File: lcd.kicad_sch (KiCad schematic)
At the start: 9 parts, among them J5 Conn_01x10

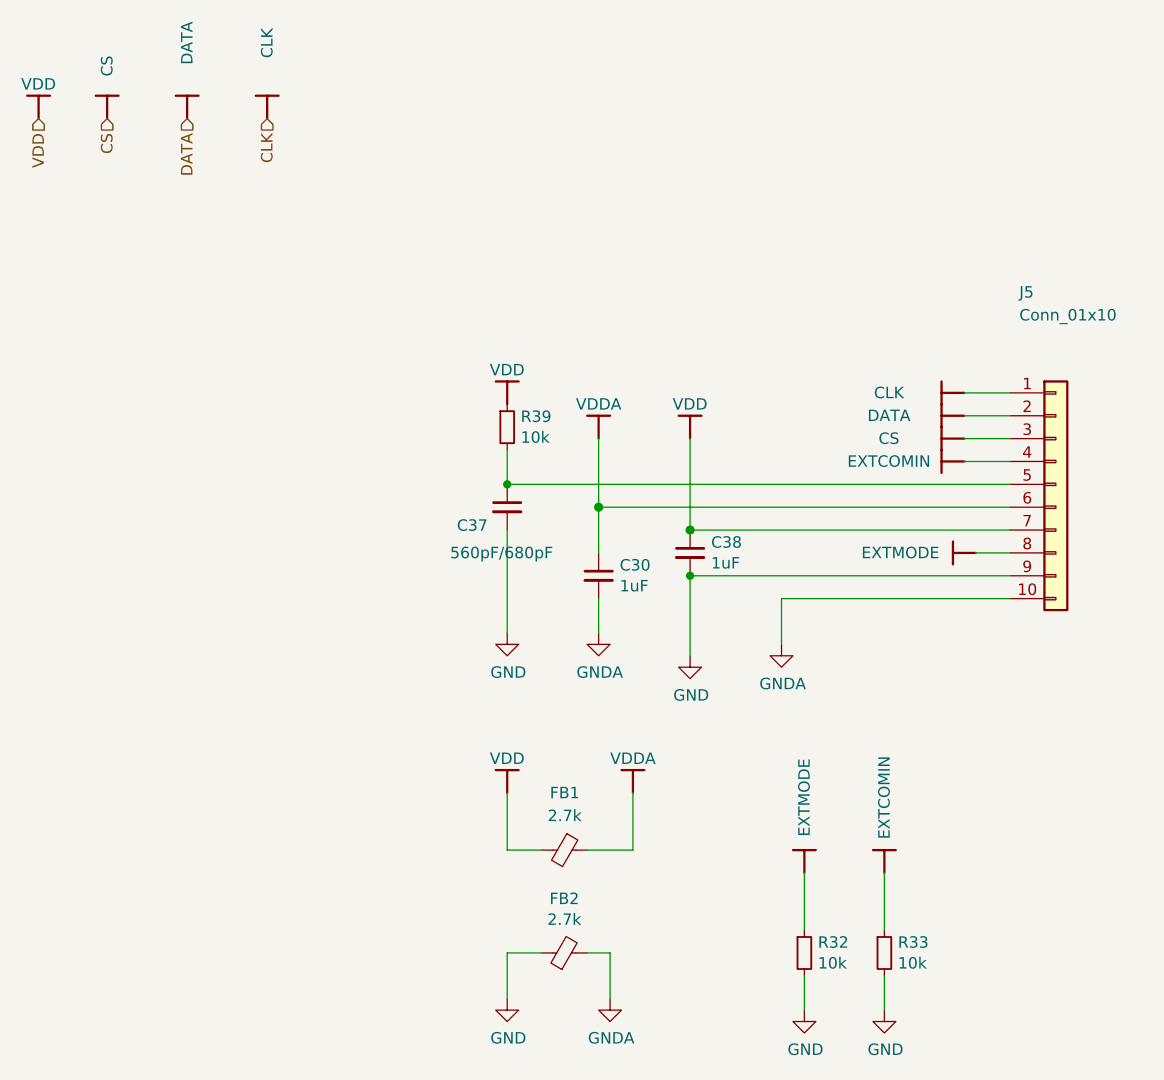
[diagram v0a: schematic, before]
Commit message: Cleaning up the LCD schematics
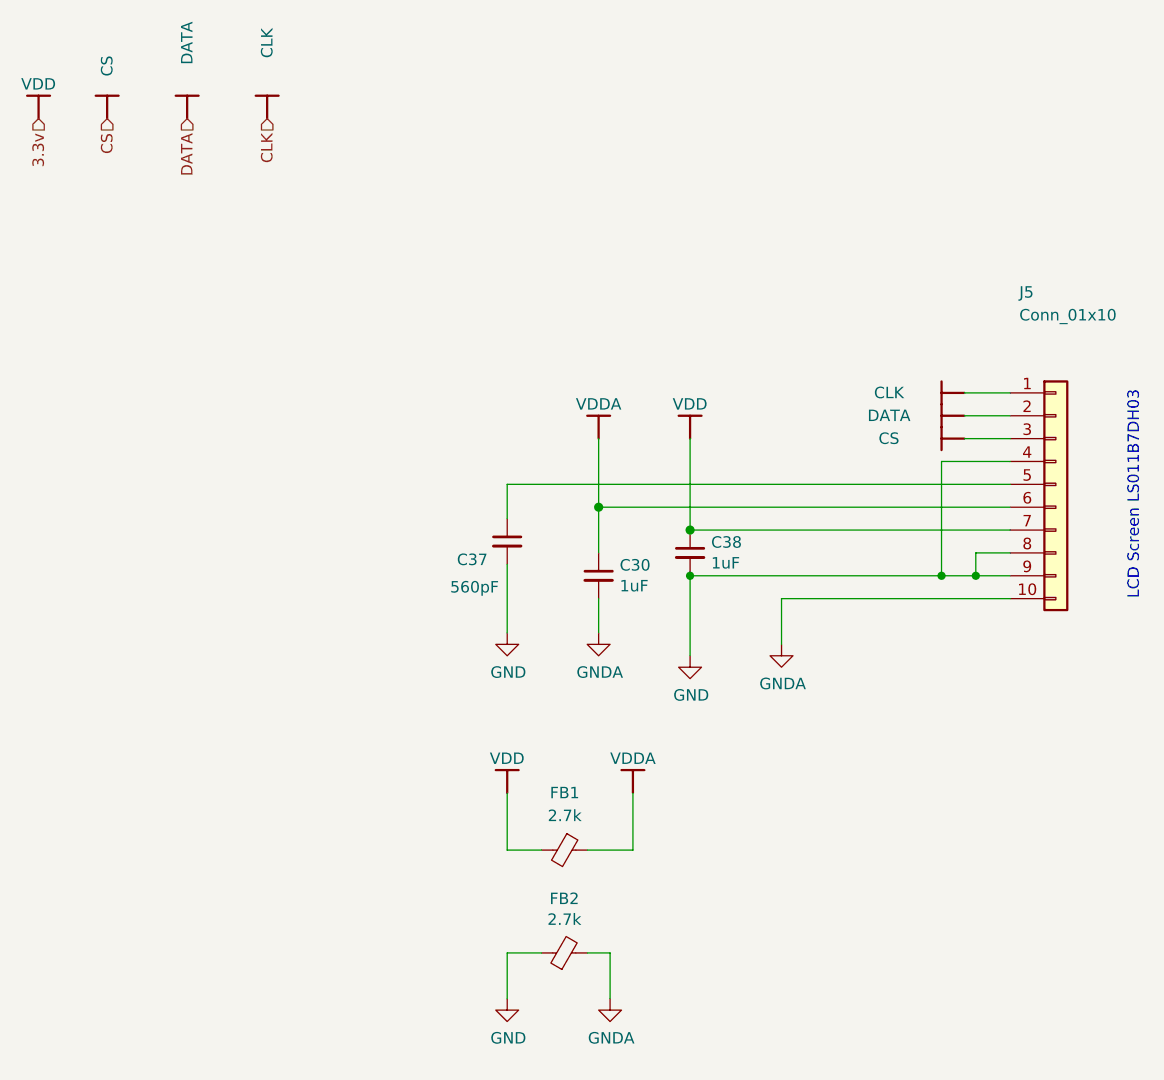
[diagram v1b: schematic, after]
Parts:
- removed R32, R33, R39: 10k, Resistor_SMD:R_0201_0603Metric, symbol Device:R_Small
- C37: value 560pF/680pF -> 560pF
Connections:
- net EXTCOMIN is gone; now on net GND: J5.4 (Pin_4)
- net EXTMODE is gone; now on net GND: J5.8 (Pin_8)
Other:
- note added: "LCD Screen LS011B7DH03"
- moved on the sheet: C37

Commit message: Re-linking the PCB properties back to the schematics
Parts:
- C30, C37, C38: footprint Capacitor_SMD:C_0201_0603Metric -> Library:C_0402_1005
- FB1, FB2: footprint Resistor_SMD:R_0402_1005Metric -> Library:R_0402_1005
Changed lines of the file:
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@@
 			)
 		)
-		(property "Footprint" "Resistor_SMD:R_0402_1005Metric"
+		(property "Footprint" "Library:R_0402_1005"
 			(at 111.76 127.508 90)
 			(effects
@@
 			)
 		)
-		(property "Footprint" "Resistor_SMD:R_0402_1005Metric"
+		(property "Footprint" "Library:R_0402_1005"
 			(at 111.76 112.522 90)
 			(effects
@@
 			)
 		)
-		(property "Footprint" "Capacitor_SMD:C_0201_0603Metric"
+		(property "Footprint" "Library:C_0402_1005"
 			(at 115.57 83.82 0)
 			(effects
@@
 			)
 		)
-		(property "Footprint" "Capacitor_SMD:C_0201_0603Metric"
+		(property "Footprint" "Library:C_0402_1005"
 			(at 105.41 80.01 0)
 			(effects
@@
 			)
 		)
-		(property "Footprint" "Capacitor_SMD:C_0201_0603Metric"
+		(property "Footprint" "Library:C_0402_1005"
 			(at 125.73 81.28 0)
 			(effects

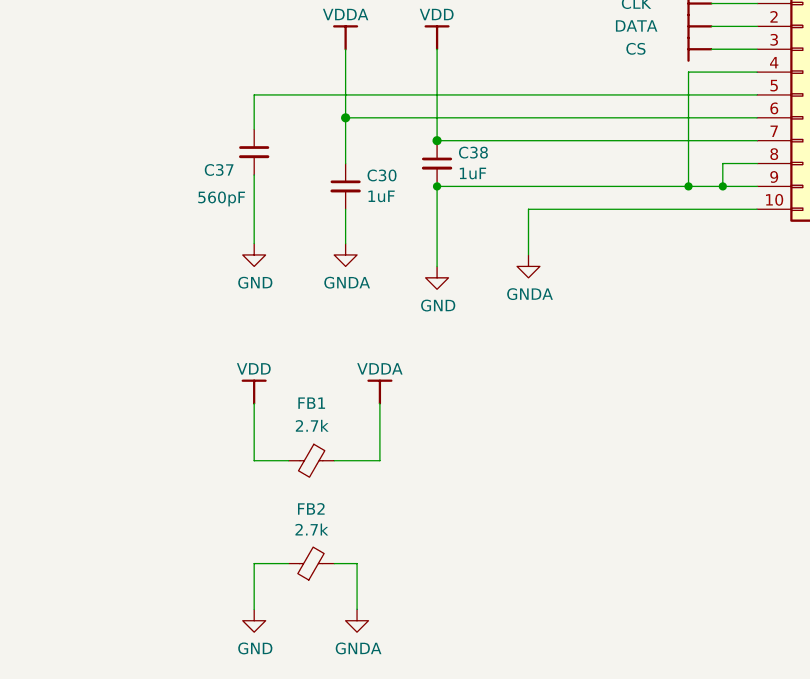
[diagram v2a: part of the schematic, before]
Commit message: Optimising for BOM and placements cost reduction
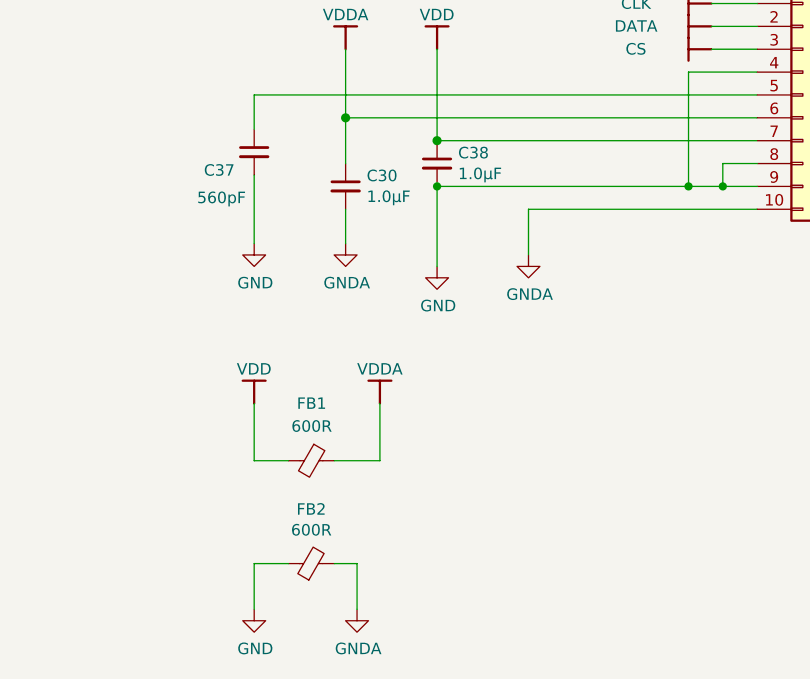
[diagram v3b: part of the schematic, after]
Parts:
- C30, C38: value 1uF -> 1.0µF
- FB1, FB2: value 2.7k -> 600R; footprint Library:R_0402_1005 -> Library:F_0603_1608
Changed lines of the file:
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@@
 			)
 		)
-		(property "Value" "2.7k"
+		(property "Value" "600R"
 			(at 111.76 122.0216 90)
 			(effects
@@
 			)
 		)
-		(property "Footprint" "Library:R_0402_1005"
+		(property "Footprint" "Library:F_0603_1608"
 			(at 111.76 127.508 90)
 			(effects
@@
 			)
 		)
-		(property "Value" "2.7k"
+		(property "Value" "600R"
 			(at 111.7981 110.49 90)
 			(effects
@@
 			)
 		)
-		(property "Footprint" "Library:R_0402_1005"
+		(property "Footprint" "Library:F_0603_1608"
 			(at 111.76 112.522 90)
 			(effects
@@
 			)
 		)
-		(property "Value" "1uF"
+		(property "Value" "1.0µF"
 			(at 117.9068 84.963 0)
 			(effects
@@
 			)
 		)
-		(property "Value" "1uF"
+		(property "Value" "1.0µF"
 			(at 128.0668 82.423 0)
 			(effects

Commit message: Further optimising the BOM and adding JLCPCB specific part numbers
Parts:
- C30, C38: LCSC C15849 -> C52923
- C37: LCSC C84721 -> C1539
- FB1, FB2: LCSC C1017 -> C1002
- J5: LCSC C506791 -> C324723
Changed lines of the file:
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@@
 			)
 		)
-		(property "LCSC" "C1017"
+		(property "LCSC" "C1002"
 			(at 111.76 125.73 0)
+			(effects
+				(font
+					(size 1.27 1.27)
+				)
+				(hide yes)
+			)
+		)
+		(property "AVAILABILITY" ""
+			(at 111.76 125.73 90)
+			(effects
+				(font
+					(size 1.27 1.27)
+				)
+				(hide yes)
+			)
+		)
+		(property "DESCRIPTION" ""
+			(at 111.76 125.73 90)
+			(effects
+				(font
+					(size 1.27 1.27)
+				)
+				(hide yes)
+			)
+		)
+		(property "PACKAGE" ""
+			(at 111.76 125.73 90)
+			(effects
+				(font
+					(size 1.27 1.27)
+				)
+				(hide yes)
+			)
+		)
+		(property "PRICE" ""
+			(at 111.76 125.73 90)
 			(effects
 				(font
@@
 			)
 		)
-		(property "LCSC" "C1017"
+		(property "LCSC" "C1002"
 			(at 111.76 114.3 0)
+			(effects
+				(font
+					(size 1.27 1.27)
+				)
+				(hide yes)
+			)
+		)
+		(property "AVAILABILITY" ""
+			(at 111.76 114.3 90)
+			(effects
+				(font
+					(size 1.27 1.27)
+				)
+				(hide yes)
+			)
+		)
+		(property "DESCRIPTION" ""
+			(at 111.76 114.3 90)
+			(effects
+				(font
+					(size 1.27 1.27)
+				)
+				(hide yes)
+			)
+		)
+		(property "PACKAGE" ""
+			(at 111.76 114.3 90)
+			(effects
+				(font
+					(size 1.27 1.27)
+				)
+				(hide yes)
+			)
+		)
+		(property "PRICE" ""
+			(at 111.76 114.3 90)
 			(effects
 				(font
@@
 			)
 		)
-		(property "Datasheet" "~"
+		(property "Datasheet" ""
 			(at 115.57 83.82 0)
 			(effects
@@
 			)
 		)
-		(property "LCSC" "C15849"
+		(property "LCSC" "C52923"
+			(at 115.57 83.82 0)
+			(effects
+				(font
+					(size 1.27 1.27)
+				)
+				(hide yes)
+			)
+		)
+		(property "AVAILABILITY" ""
+			(at 115.57 83.82 0)
+			(effects
+				(font
+					(size 1.27 1.27)
+				)
+				(hide yes)
+			)
+		)
+		(property "DESCRIPTION" ""
+			(at 115.57 83.82 0)
+			(effects
+				(font
+					(size 1.27 1.27)
+				)
+				(hide yes)
+			)
+		)
+		(property "PACKAGE" ""
+			(at 115.57 83.82 0)
+			(effects
+				(font
+					(size 1.27 1.27)
+				)
+				(hide yes)
+			)
+		)
+		(property "PRICE" ""
 			(at 115.57 83.82 0)
 			(effects
@@
 			)
 		)
-		(property "LCSC" "C84721"
+		(property "LCSC" "C1539"
+			(at 105.41 80.01 0)
+			(effects
+				(font
+					(size 1.27 1.27)
+				)
+				(hide yes)
+			)
+		)
+		(property "AVAILABILITY" ""
+			(at 105.41 80.01 0)
+			(effects
+				(font
+					(size 1.27 1.27)
+				)
+				(hide yes)
+			)
+		)
+		(property "DESCRIPTION" ""
+			(at 105.41 80.01 0)
+			(effects
+				(font
+					(size 1.27 1.27)
+				)
+				(hide yes)
+			)
+		)
+		(property "PACKAGE" ""
+			(at 105.41 80.01 0)
+			(effects
+				(font
+					(size 1.27 1.27)
+				)
+				(hide yes)
+			)
+		)
+		(property "PRICE" ""
 			(at 105.41 80.01 0)
 			(effects
@@
 			)
 		)
-		(property "LCSC" "C506791"
+		(property "LCSC" "C324723"
+			(at 166.37 73.66 0)
+			(effects
+				(font
+					(size 1.27 1.27)
+				)
+				(hide yes)
+			)
+		)
+		(property "AVAILABILITY" ""
+			(at 166.37 73.66 0)
+			(effects
+				(font
+					(size 1.27 1.27)
+				)
+				(hide yes)
+			)
+		)
+		(property "DESCRIPTION" ""
+			(at 166.37 73.66 0)
+			(effects
+				(font
+					(size 1.27 1.27)
+				)
+				(hide yes)
+			)
+		)
+		(property "PACKAGE" ""
+			(at 166.37 73.66 0)
+			(effects
+				(font
+					(size 1.27 1.27)
+				)
+				(hide yes)
+			)
+		)
+		(property "PRICE" ""
 			(at 166.37 73.66 0)
 			(effects
@@
 			)
 		)
-		(property "Datasheet" "~"
+		(property "Datasheet" ""
 			(at 125.73 81.28 0)
 			(effects
@@
 			)
 		)
-		(property "LCSC" "C15849"
+		(property "LCSC" "C52923"
 			(at 125.73 81.28 0)
 			(effects
+				(font
+					(size 1.27 1.27)
+				)
+				(hide yes)
+			)
+		)
+		(property "AVAILABILITY" ""
+			(at 125.73 81.28 0)
+			(effects
+				(font
+					(size 1.27 1.27)
+				)
+				(hide yes)
+			)
+		)
+		(property "DESCRIPTION" ""
+			(at 125.73 81.28 0)
+			(effects
+				(font
+					(size 1.27 1.27)
+				)
+				(hide yes)
+			)
+		)
+		(property "PACKAGE" ""
+			(at 125.73 81.28 0)
+			(effects
+				(font
+					(size 1.27 1.27)
+				)
+				(hide yes)
+			)
+		)
+		(property "PRICE" ""
+			(at 125.73 81.28 0)
+			(effects

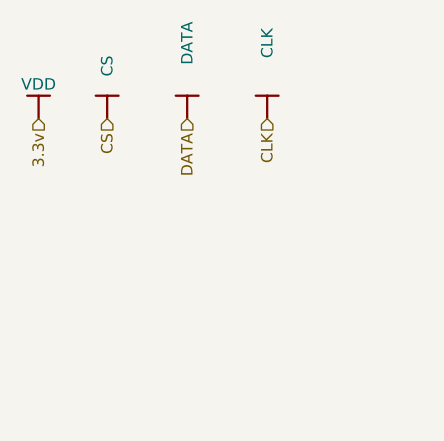
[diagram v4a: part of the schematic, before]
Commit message: Removing the 1.8v power supply option
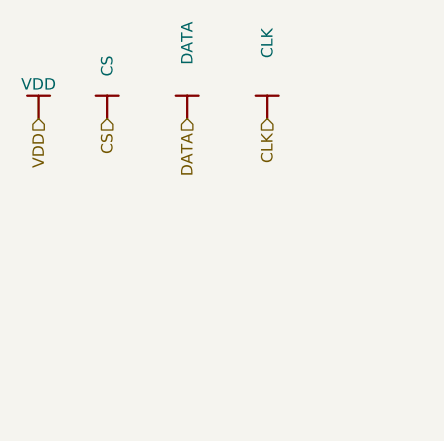
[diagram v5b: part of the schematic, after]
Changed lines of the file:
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@@
 		)
 	)
-	(hierarchical_label "3.3v"
+	(hierarchical_label "VDD"
 		(shape input)
 		(at 53.34 33.02 270)
